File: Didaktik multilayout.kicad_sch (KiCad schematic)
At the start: 119 parts, among them J1 Conn_01x04_MountingPin, J2 AVR-ISP-6, SW1 SW_Push_45deg, SW10 SW_Push_45deg, SW11 SW_Push_45deg, SW12 SW_Push_45deg, SW13 SW_Push_45deg, SW14 SW_Push_45deg, SW15 SW_Push_45deg, SW16 SW_Push_45deg, SW17 SW_Push_45deg, SW18 SW_Push_45deg, SW19 SW_Push_45deg, SW2 SW_Push_45deg, SW20 SW_Push_45deg, SW21 SW_Push_45deg, SW22 SW_Push_45deg, SW23 SW_Push_45deg, SW24 SW_Push_45deg, SW25 SW_Push_45deg, SW26 SW_Push_45deg, SW27 SW_Push_45deg, SW28 SW_Push_45deg, SW29 SW_Push_45deg, SW3 SW_Push_45deg, SW30 SW_Push_45deg, SW31 SW_Push_45deg, SW31a1 SW_Push_45deg, SW32 SW_Push_45deg, SW32a1 SW_Push_45deg, SW33 SW_Push_45deg, SW33a1 SW_Push_45deg, SW34 SW_Push_45deg, SW34a1 SW_Push_45deg, SW34b1 SW_Push_45deg, SW35 SW_Push_45deg, SW35a1 SW_Push_45deg, SW35b1 SW_Push_45deg, SW35c1 SW_Push_45deg, SW36 SW_Push_45deg, SW36a1 SW_Push_45deg, SW36b1 SW_Push_45deg, SW36c1 SW_Push_45deg, SW37 SW_Push_45deg, SW37a1 SW_Push_45deg, SW37b1 SW_Push_45deg, SW38 SW_Push_45deg, SW38a1 SW_Push_45deg, SW39 SW_Push_45deg, SW39a1 SW_Push_45deg, SW4 SW_Push_45deg, SW40 SW_Push_45deg, SW40a1 SW_Push_45deg, SW5 SW_Push_45deg, SW6 SW_Push_45deg, SW7 SW_Push_45deg, SW8 SW_Push_45deg, SW9 SW_Push_45deg, U1 ATmega32U4-M, Y1 Crystal_GND24_Small

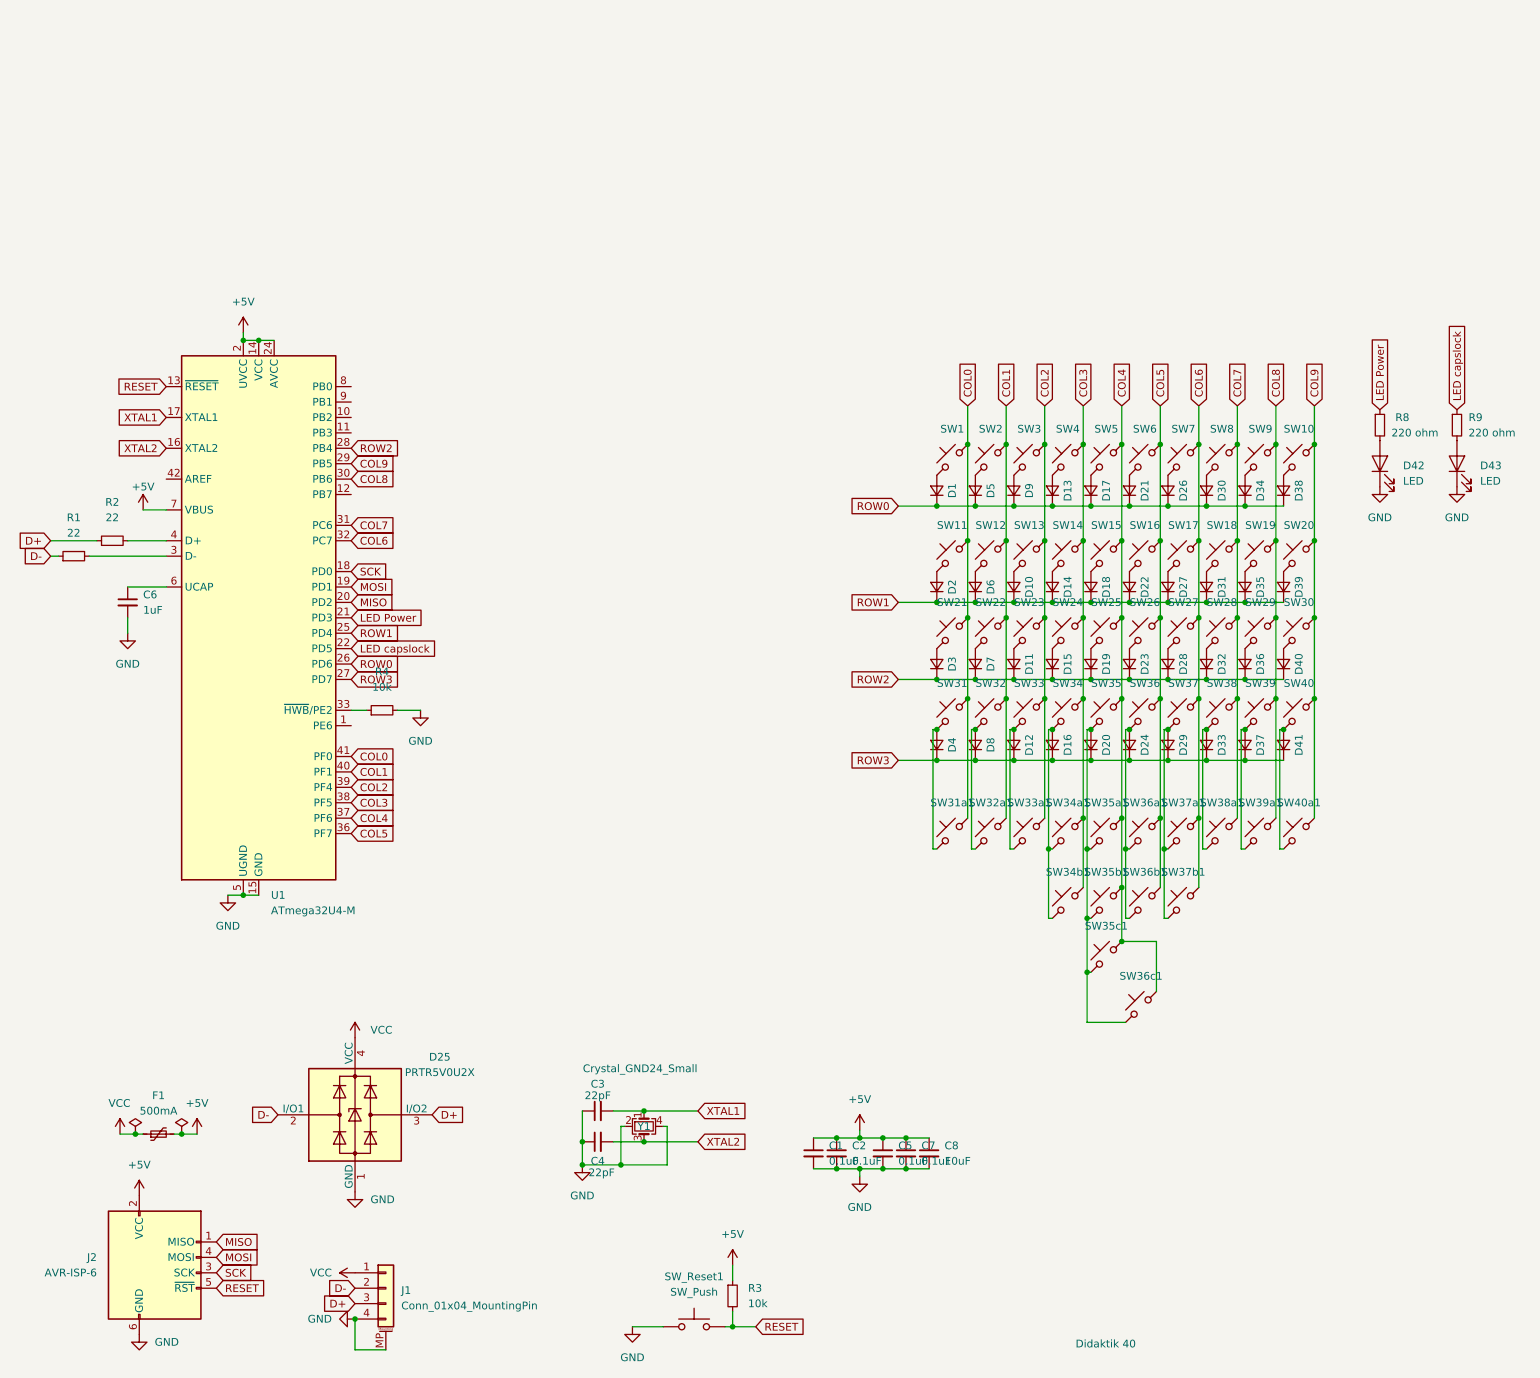
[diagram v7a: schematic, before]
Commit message: adding rotaries & rgb breakout
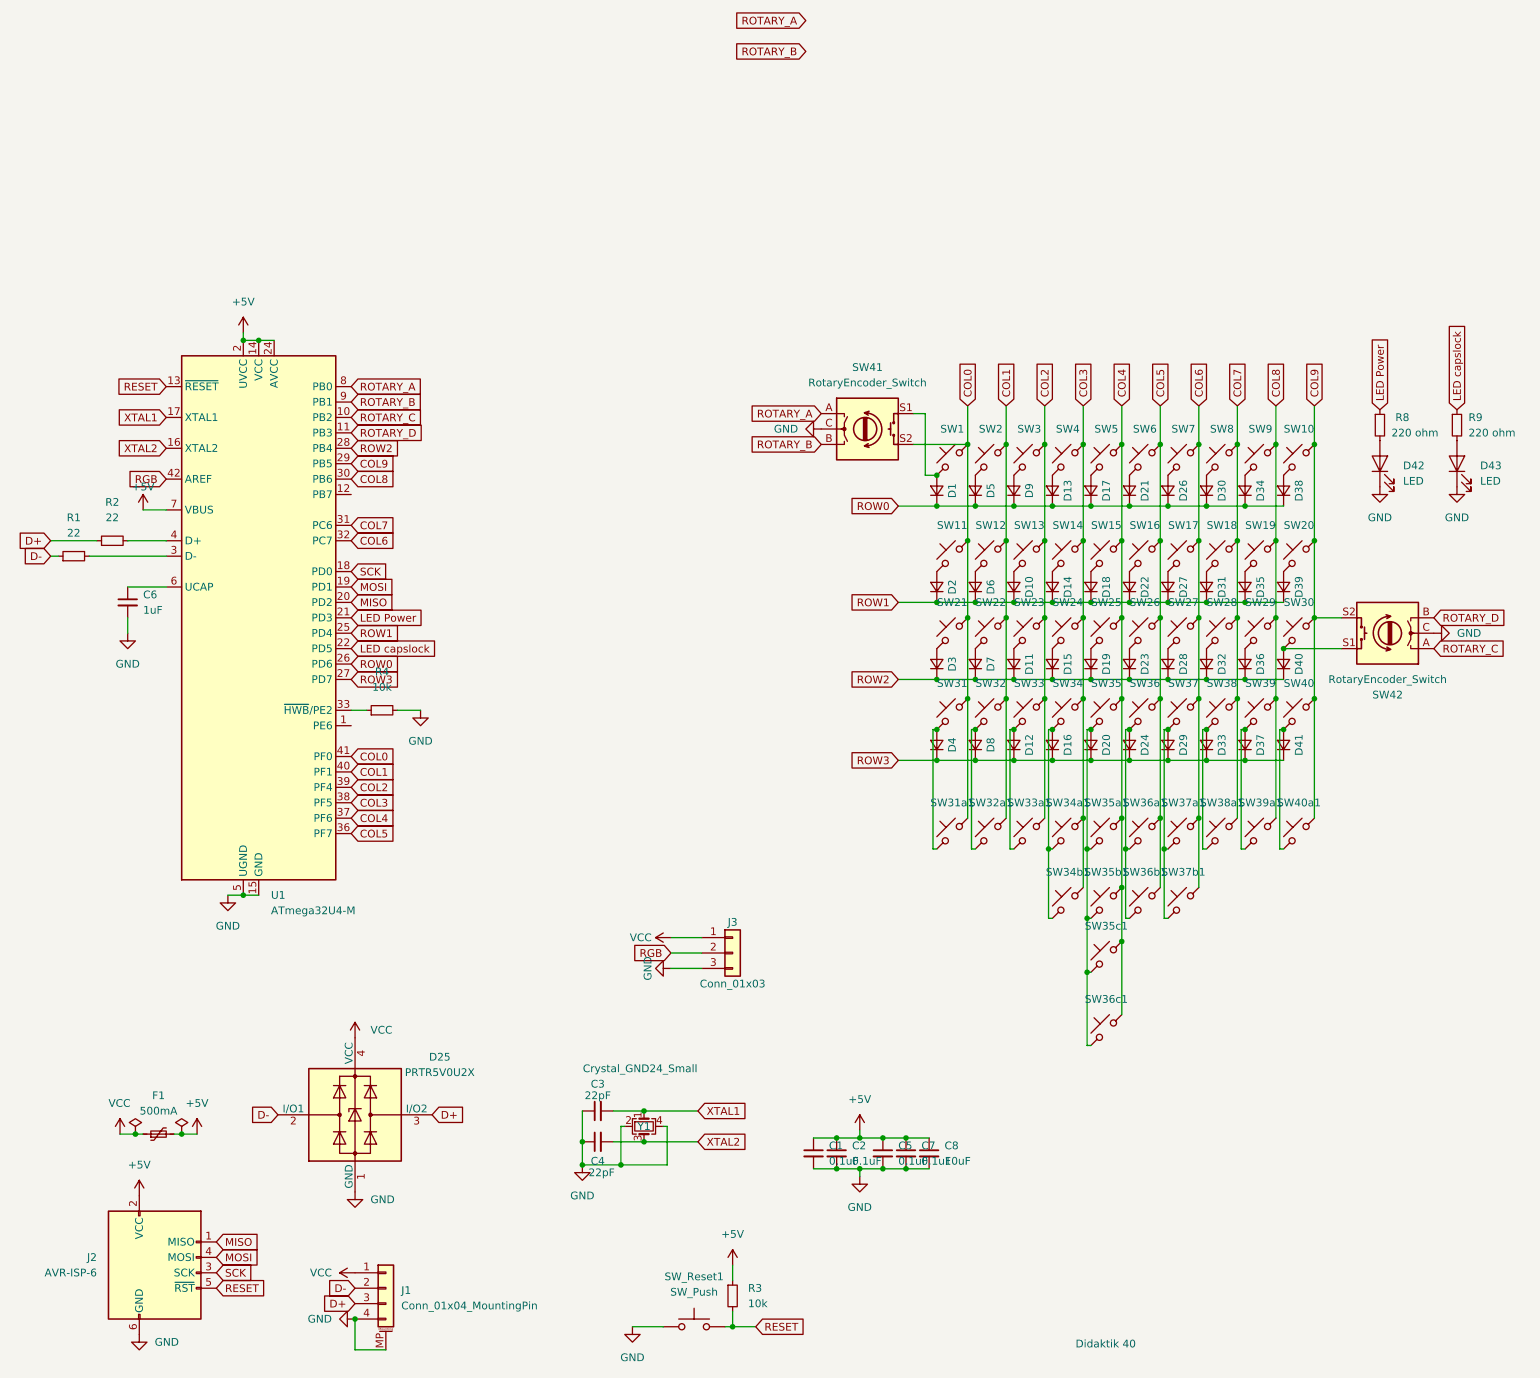
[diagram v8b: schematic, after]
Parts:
- added J3: Conn_01x03, Connector_PinHeader_2.54mm:PinHeader_1x03_P2.54mm_Vertical, symbol alpha_pro_micro-rescue:Conn_01x03
- added SW41, SW42: RotaryEncoder_Switch, Keebio-Parts:RotaryEncoder_Alps_EC11E-Switch_Vertical_H20mm, symbol Device:RotaryEncoder_Switch
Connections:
- net COL0: now also SW41.S2
- net COL9: now also SW42.S2
- net GND: now also J3.3 (Pin_3), SW41.C, SW42.C
- net VCC: now also J3.1 (Pin_1)
- net ROTARY_C: now reaches U1.10 (PB2)
- net ROTARY_C: now also SW42.A
- net ROTARY_D: now reaches U1.11 (PB3)
- net ROTARY_D: now also SW42.B
- net RGB: now reaches U1.42 (AREF)
- net RGB: now also J3.2 (Pin_2)
- net ROTARY_A: now reaches U1.8 (PB0)
- net ROTARY_A: now also SW41.A
- net ROTARY_B: now reaches U1.9 (PB1)
- net ROTARY_B: now also SW41.B
- net at D1.2 (A), SW1.2: now also SW41.S1
- net at D40.2 (A), SW30.2: now also SW42.S1
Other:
- moved on the sheet: SW36c1
